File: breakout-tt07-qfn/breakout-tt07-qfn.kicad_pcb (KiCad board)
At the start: 2 copper layers, 50 x 52 mm, 153 parts, among them J1 Conn_01x04, J10 U.FL, J11 U.FL, J12 U.FL, J13 U.FL, J2 U.FL, J3 U.FL, J4 U.FL, J5 U.FL, J6 U.FL, J7 U.FL, J8 U.FL, J9 U.FL, U1 Openframe_QFN_TT06_REV2, U2 24LC02

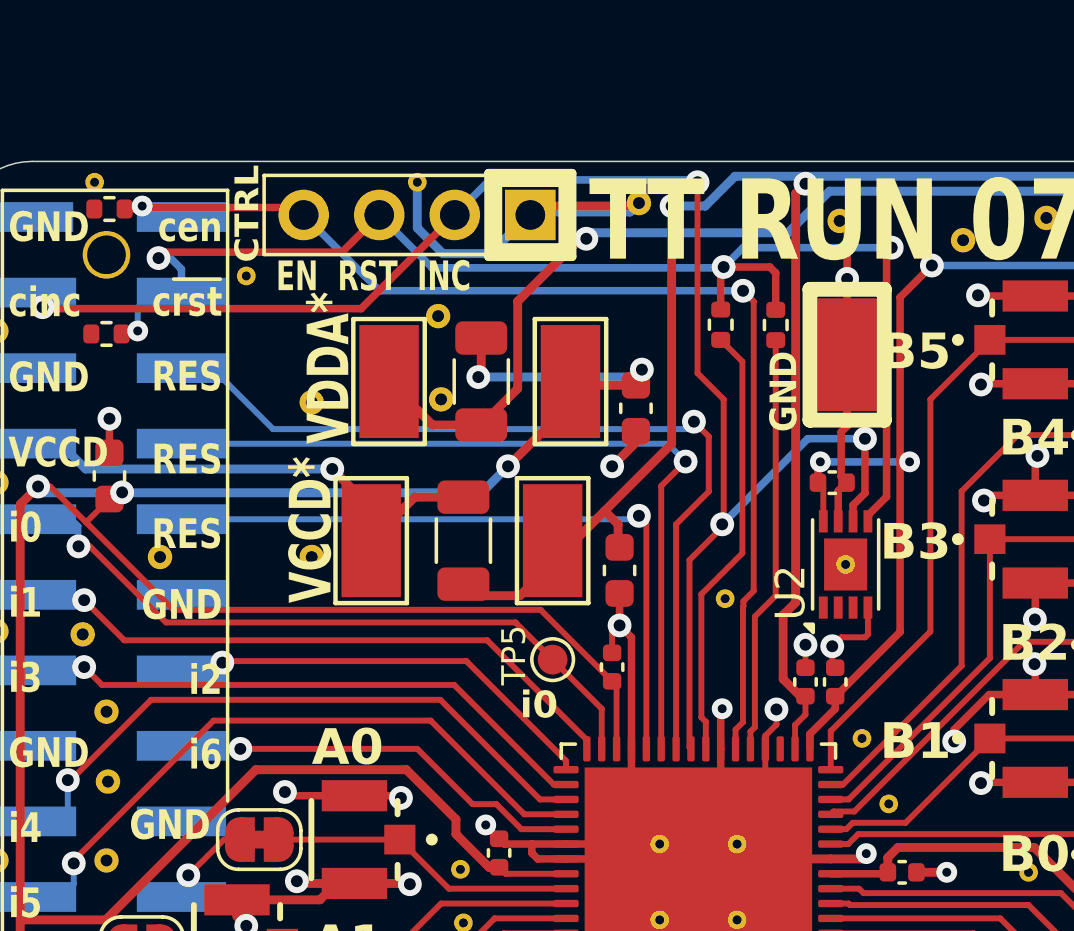
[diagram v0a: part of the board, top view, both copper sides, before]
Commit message: fix for mystery regression on MUX rst/sel lines
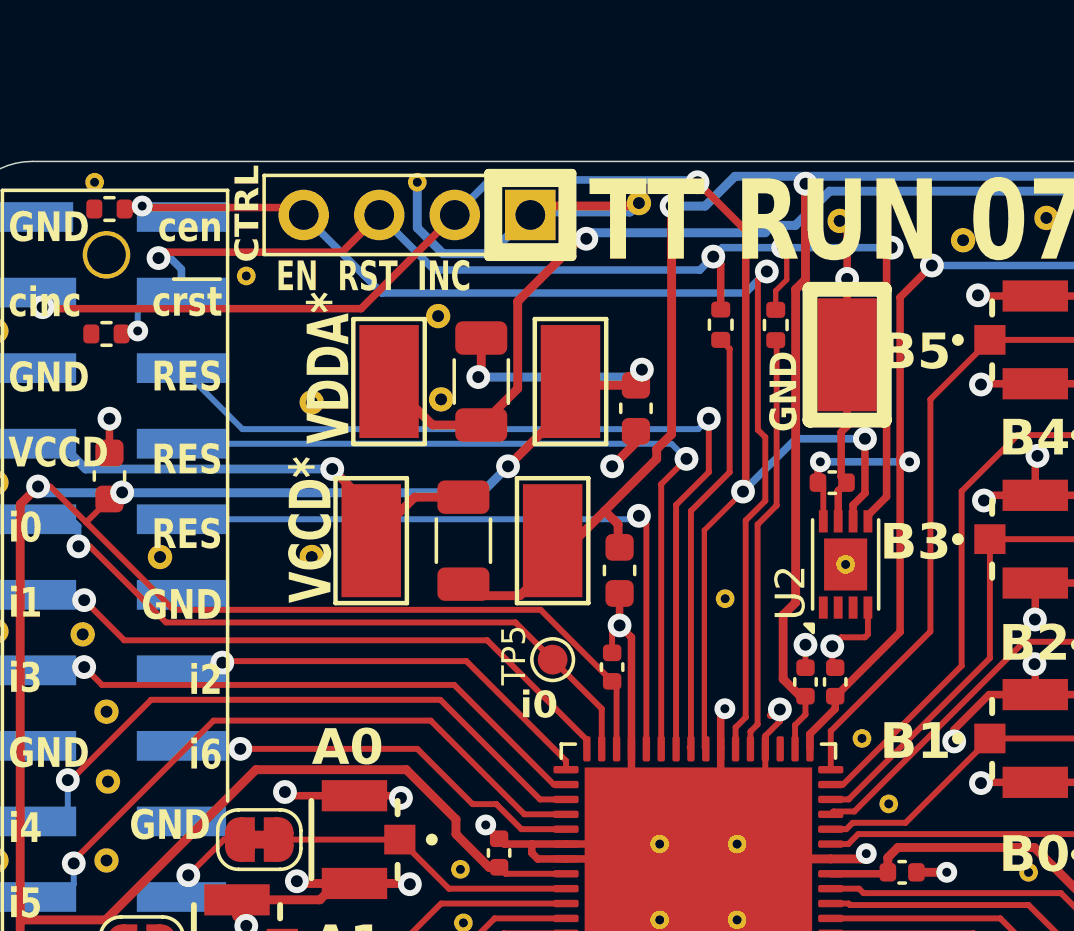
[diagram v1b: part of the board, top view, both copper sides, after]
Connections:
- U1 pad 24: /c_rst_n -> /c_sel_inc
- U1 pad 25: /c_sel_inc -> /c_rst_n
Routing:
- net /c_ena: track 38.4 -> 40.4 mm
- net /c_sel_inc: track 53.4 -> 52.6 mm
- net /hd_c_rst_n: track 45.1 -> 44.8 mm, vias 4 -> 5
